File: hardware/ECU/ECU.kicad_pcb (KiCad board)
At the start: 2 copper layers, 148 x 111.5 mm, 162 parts, among them IC1 MAX9926UAEE_V+, IC2 ZXMS6006DT8, IC3 ZXMS6006DT8, IC4 ZXMS6006DT8, J1 Conn_01x04, Q1 Q_DUAL_NMOS_S1G1D2S2G2D1, Q2 Q_DUAL_NMOS_S1G1D2S2G2D1, Q3 Q_PNP_BCEC, Q4 IRFB4110PBF, Q5 IRFB4110PBF, Q6 IRFB4110PBF, Q7 IRFB4110PBF, SW1 SW_DPDT_x2, SW2 SW_DPDT_x2, SW4 SW_DPDT_x2, U1 Teensy4.1, U12 LMV324LIDT, U13 SP720, U14 LMV324LIDT, U15 MC33814, U16 TC4424A, U17 W25Q32JVSS, U3 74AHC1G32, U4 ADXL343, U5 TC4424A, U7 MC33810, U9 TC4424A

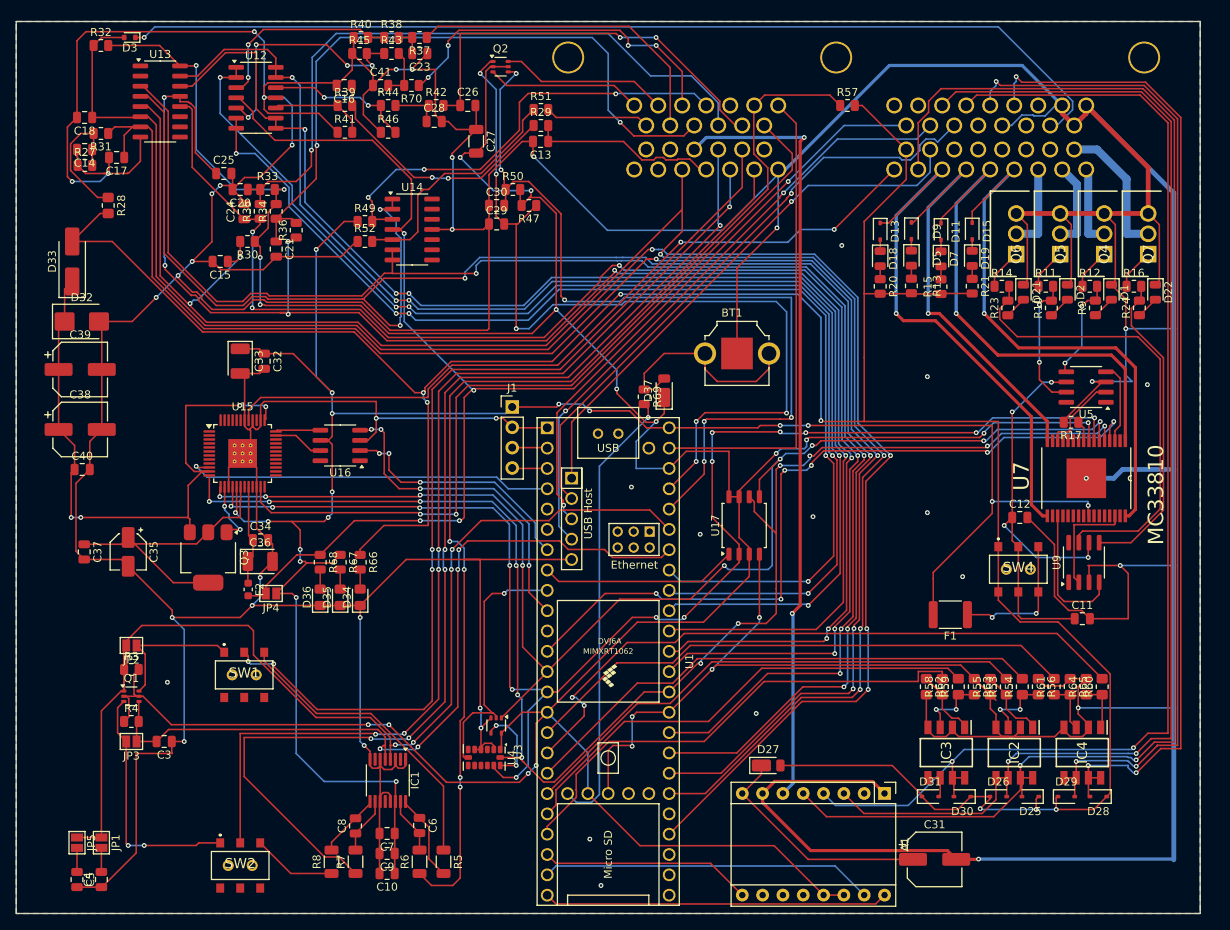
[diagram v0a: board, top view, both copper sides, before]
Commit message: Replace speeduino submodule with HasiKe fork, fix teensy.pretty path
- Switch speeduino from speeduino/speeduino to HasiKe/speeduino
- Fix teensy.pretty submodule path case mismatch (Hardware -> hardware)
- Add ISL9V5036P3-F085 component library
- Various ECU schematic updates
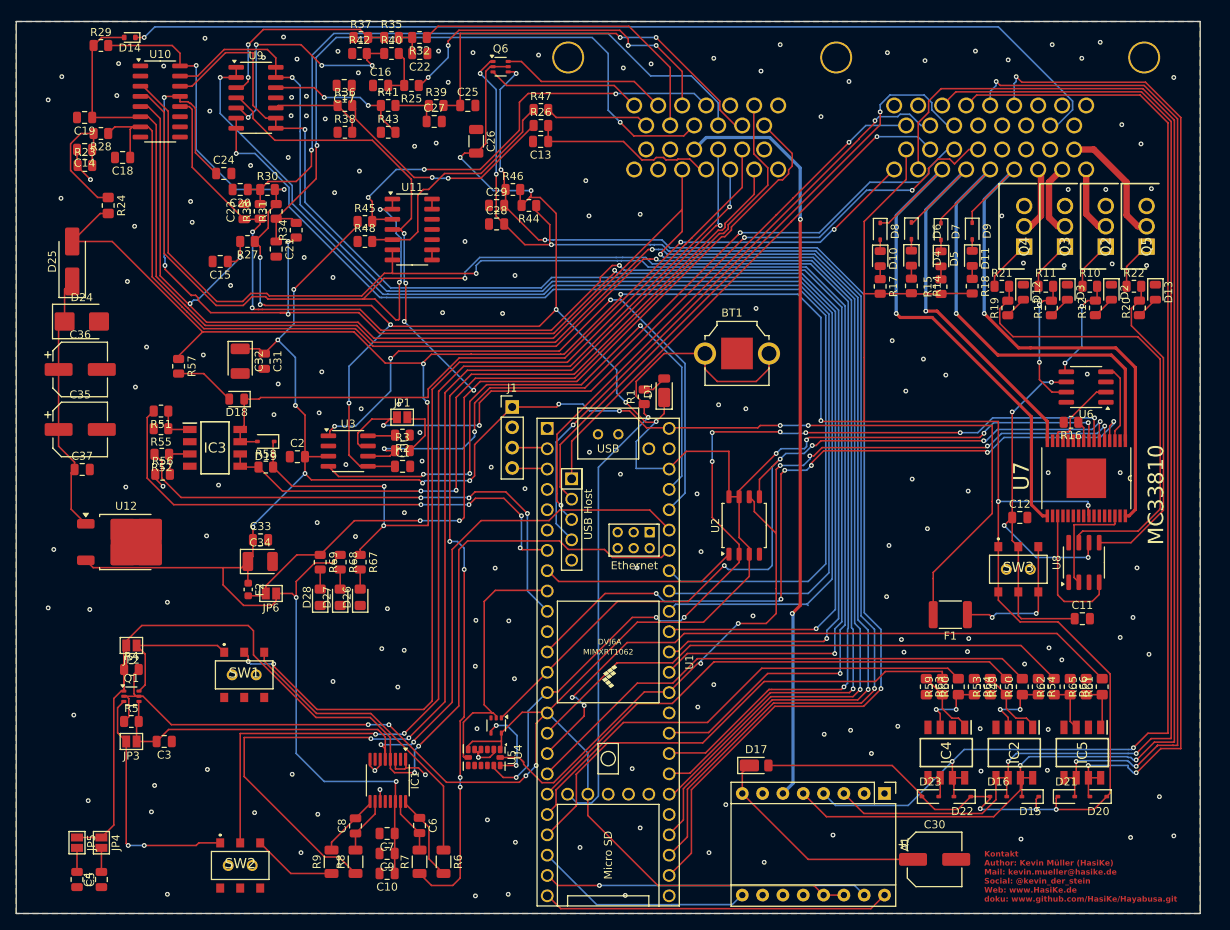
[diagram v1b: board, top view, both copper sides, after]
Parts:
- removed the C35 at (79.0, 98.3)
- removed the C37 at (73.5, 98.3)
- removed the Q6 at (190.0, 61.1)
- removed Q7: IRFB4110PBF, LIB_IRFB4110PBF:TO254P483X1016X1994-3P
- removed U15: MC33814, Package_QFP:LQFP-48-1EP_7x7mm_P0.5mm_EP3.6x3.6mm_ThermalVias
- removed U16: TC4424A, Package_SO:SOIC-8_3.9x4.9mm_P1.27mm
- added C1: 0.1uF, Capacitor_SMD:C_0805_2012Metric, F.Cu at (113.3, 87.6)
- added C2: 0.1uF, Capacitor_SMD:C_0805_2012Metric, F.Cu at (100.2, 86.4)
- added D18: LED, LED_SMD:LED_0805_2012Metric, F.Cu at (92.6, 79.2)
- added D19: D, Diode_SMD:D_SOD-323, F.Cu at (96.2, 84.5)
- added IC3: ZXMS6006DT8, ZXMS6006DT8TA:SOT153P700X170-8N, F.Cu at (89.8, 85.3)
- added JP1: Jumper_NO_Small, Jumper:SolderJumper-2_P1.3mm_Open_Pad1.0x1.5mm, F.Cu at (113.2, 81.5)
- added Q2: ISL9V5036P3-F085, ISL9V5036P3-F085:TO254P470X1016X2019-3P, F.Cu at (201.2, 60.1)
- added R2: 0R, Resistor_SMD:R_0805_2012Metric, F.Cu at (113.3, 83.7)
- added R3: 120R, Resistor_SMD:R_0805_2012Metric, F.Cu at (113.3, 85.7)
- added R51: 1k, Resistor_SMD:R_0805_2012Metric, F.Cu at (83.1, 80.7)
- added R52: 1k, Resistor_SMD:R_0805_2012Metric, F.Cu at (83.2, 86.1)
- added R55: 100k, Resistor_SMD:R_0805_2012Metric, F.Cu at (83.1, 82.9)
- added R56: 100k, Resistor_SMD:R_0805_2012Metric, F.Cu at (83.3, 88.6)
- added R58: 10k, Resistor_SMD:R_0805_2012Metric, F.Cu at (96.2, 87.7)
- added U12: MC78M05_TO252, Package_TO_SOT_SMD:TO-252-2, F.Cu at (78.7, 97.1)
- added U3: MCP2562-E-SN, Package_SO:SOIC-8_3.9x4.9mm_P1.27mm, F.Cu at (106.5, 85.7)
- Q3: value Q_PNP_BCEC -> ISL9V5036P3-F085; footprint Package_TO_SOT_SMD:SOT-223-3_TabPin2 -> ISL9V5036P3-F085:TO254P470X1016X2019-3P
- Q4, Q5: value IRFB4110PBF -> ISL9V5036P3-F085; footprint LIB_IRFB4110PBF:TO254P483X1016X1994-3P -> ISL9V5036P3-F085:TO254P470X1016X2019-3P
- R57: value 10k -> 1k
- moved Q3 113.9 mm to (196.1, 60.1), turned to 90 degrees
- moved R57 89.7 mm to (85.3, 75.1), turned to -90 degrees
- moved Q5 10.8 mm to (206.3, 60.1)
- moved Q4 10.0 mm to (191.0, 60.1)
- moved D17 1.50 mm to (157.5, 125.0)
- moved C18 0.75 mm to (78.3, 49.0)
- moved U1 0.08 mm to (139.0, 112.1)
- turned R1 to 90 degrees
- renumbered C41 to C16, C16 to C17, C17 to C18, C18 to C19, C23 to C22, C24 to C23, C25 to C24, C26 to C25, C27 to C26, C28 to C27, C29 to C28, C30 to C29, C31 to C30, C32 to C31, C33 to C32, C34 to C33, C36 to C34, C38 to C35, C39 to C36, C40 to C37, D37 to D1, D18 to D10, D19 to D11, D21 to D12, D22 to D13, D3 to D14, D25 to D15, D26 to D16, D27 to D17, D1 to D2, D28 to D20, D29 to D21, D30 to D22, D31 to D23, D32 to D24, D33 to D25, D34 to D26, D35 to D27, D36 to D28, D2 to D3, D5 to D4, D7 to D5, D9 to D6, D11 to D7, D13 to D8, D15 to D9, IC3 to IC4, IC4 to IC5, J5 to J2, JP1 to JP4, JP4 to JP6, Q2 to Q6, R69 to R1, R12 to R10, R9 to R12, R10 to R13, R13 to R14, R17 to R16, R20 to R17, R21 to R18, R23 to R19, R24 to R20, R14 to R21, R16 to R22, R27 to R23, R28 to R24, R70 to R25, R29 to R26, R30 to R27, R31 to R28, R32 to R29, R33 to R30, R34 to R31, R37 to R32, R35 to R33, R36 to R34, R38 to R35, R39 to R36, R40 to R37, R41 to R38, R42 to R39, R3 to R4, R43 to R40, R44 to R41, R45 to R42, R46 to R43, R47 to R44, R49 to R45, R50 to R46, R51 to R47, R52 to R48, R53 to R49, R4 to R5, R54 to R50, R55 to R53, R56 to R54, R58 to R59, R5 to R6, R59 to R60, R60 to R61, R61 to R62, R62 to R63, R63 to R64, R64 to R65, R65 to R66, R66 to R67, R67 to R68, R68 to R69, R6 to R7, R7 to R8, R8 to R9, SW4 to SW3, U13 to U10, U14 to U11, U17 to U2, U3 to U4, U4 to U5, U5 to U6, U9 to U8, U12 to U9
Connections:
- C28 pad 2: MCU-D23 -> MCU-D35
- C29 pad 2: MCU-D22 -> MCU-D34
- C3 pad 2: MCU-D18 -> MCU-D21
- C33 pad 1: Net-(U15-VPROT) -> +5V
- C34 pad 1: Net-(U15-VPROT) -> +5V
- F2 pad 1: Net-(U15-VPROT) -> +5V
- IC1 pad 4: MCU-D19 -> MCU-D20
- IC1 pad 5: MCU-D18 -> MCU-D21
- J2 pad 54: GNDA -> GND
- J2 pad 55: ROUT2 -> TACHO-OUT
- JP2 pad 2: MCU-D19 -> MCU-D20
- JP3 pad 1: MCU-D18 -> MCU-D21
- JP4 pad 1: MCU-D19 -> MCU-D20
- JP5 pad 1: MCU-D19 -> MCU-D20
- Q1 pad 1: MCU-D19 -> MCU-D20
- Q1 pad 4: MCU-D18 -> MCU-D21
- Q3 pad 1: VPPREF -> Net-(Q3-Pad1)
- Q3 pad 2: VPPSENS -> IGN2
- Q3 pad 3: 12V-PROT -> GND
- Q4 pad 1: Net-(Q4-G) -> Net-(Q4-Pad1)
- Q4 pad 2: IGN1 -> IGN3
- Q5 pad 1: Net-(Q5-G) -> Net-(Q5-Pad1)
- Q5 pad 2: IGN2 -> IGN4
- Q6 pad 1: MCU-D23 -> MCU-D35
- Q6 pad 4: MCU-D22 -> MCU-D34
- R10 pad 1: Net-(Q4-G) -> Net-(Q2-Pad1)
- R11 pad 1: Net-(Q5-G) -> Net-(Q3-Pad1)
- R21 pad 1: Net-(Q6-G) -> Net-(Q4-Pad1)
- R22 pad 1: Net-(Q7-G) -> Net-(Q5-Pad1)
- R4 pad 1: MCU-D19 -> MCU-D20
- R44 pad 1: MCU-D23 -> MCU-D35
- R46 pad 1: MCU-D22 -> MCU-D34
- R5 pad 2: MCU-D18 -> MCU-D21
- R57 pad 1: ROUT2 -> 12V-SW
- R57 pad 2: 12V-SW -> Net-(D18-A)
- U1 pad 26: unconnected-(U1-34_RX8-Pad26) -> MCU-D34
- U1 pad 27: unconnected-(U1-35_TX8-Pad27) -> MCU-D35
- U1 pad 42: MCU-D18 -> MCU-D20
- U1 pad 43: MCU-D19 -> MCU-D21
- U1 pad 47: GNDA -> GND
- U7 pad 25: +5V -> 12V-SW
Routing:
- net GND: track 1206.3 -> 22.6 mm, vias 48 -> 176
- net MCU-D35: track 0.00 -> 164.1 mm, vias 0 -> 4
- net MCU-D34: track 0.00 -> 159.3 mm, vias 0 -> 4
- net MCU-D20: track 0.00 -> 141.6 mm, vias 0 -> 2
- net MCU-D19: track 138.4 -> 0.00 mm, vias 4 -> 0
- net ROUT2: track 114.5 -> 0.00 mm, vias 2 -> 0
- net MCU-D21: track 0.00 -> 102.6 mm, vias 0 -> 2
- net TACHO-OUT: track 0.00 -> 102.4 mm, vias 0 -> 2
- net CAN_H: track 0.00 -> 101.8 mm, vias 0 -> 4
- net MCU-D18: track 100.5 -> 0.00 mm, vias 4 -> 0
- net CAN_L: track 0.00 -> 94.8 mm, vias 0 -> 3
- net SCLK: track 187.0 -> 114.7 mm, vias 12 -> 6
- net MISO: track 179.8 -> 116.7 mm, vias 14 -> 9
- net MOSI: track 166.6 -> 106.2 mm, vias 9 -> 5
- net GNDA: track 59.6 -> 0.00 mm
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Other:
- board text added: "Kontakt Author: Kevin Müller (HasiKe) Mail: kevin.mueller@hasike.de Social: @kevin_der_stein Web: www.HasiKe.de doku: www.github.com/HasiKe/Hayabusa.git"
